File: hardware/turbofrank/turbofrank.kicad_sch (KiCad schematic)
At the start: 7 parts, among them CON2 UART, CON4 Power, J1 Main Jumper Set

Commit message: HW Rev 1.0
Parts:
- CON1: renamed from CON2; value UART -> Pin Header 1x03; AliExpress (none) -> https://www.aliexpress.com/item/1005007039504981.html
- CON2: renamed from CON4; value Power -> Pin Header 1x03; AliExpress (none) -> https://www.aliexpress.com/item/1005007039504981.html
- H1, H2, H3, H4: value MountingHole -> Hole 2.7mm
- J1: value Main Jumper Set -> Pin Header 2x18; AliExpress (none) -> https://www.aliexpress.com/item/1005006804478835.html
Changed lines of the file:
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@@
 	(title_block
 		(title "TurboFRANK")
-		(date "2025-01-28")
+		(date "2025-01-29")
 		(rev "1.0")
 		(company "Mikhail Matveev")
@@
 		(dnp no)
 		(fields_autoplaced yes)
-		(property "Reference" "#PWR0113"
+		(property "Reference" "#PWR05"
 			(at 201.93 102.87 0)
 			(effects
@@
 			(project ""
 				(path "/8c0b3d8b-46d3-4173-ab1e-a61765f77d61"
-					(reference "#PWR0113")
+					(reference "#PWR05")
 					(unit 1)
 				)
@@
 		(dnp no)
 		(fields_autoplaced yes)
-		(property "Reference" "CON2"
+		(property "Reference" "CON1"
 			(at 201.295 77.47 0)
 			(effects
@@
 			)
 		)
-		(property "Value" "UART"
+		(property "Value" "Pin Header 1x03"
 			(at 201.295 80.01 0)
 			(effects
@@
 			)
 		)
+		(property "AliExpress" "https://www.aliexpress.com/item/1005007039504981.html"
+			(at 200.66 85.09 0)
+			(effects
+				(font
+					(size 1.27 1.27)
+				)
+				(hide yes)
+			)
+		)
 		(pin "2"
 		)
@@
 			(project ""
 				(path "/8c0b3d8b-46d3-4173-ab1e-a61765f77d61"
-					(reference "CON2")
+					(reference "CON1")
 					(unit 1)
 				)
@@
 		(dnp no)
 		(fields_autoplaced yes)
-		(property "Reference" "#PWR0112"
+		(property "Reference" "#PWR03"
 			(at 201.93 97.79 0)
 			(effects
@@
 			(project ""
 				(path "/8c0b3d8b-46d3-4173-ab1e-a61765f77d61"
-					(reference "#PWR0112")
+					(reference "#PWR03")
 					(unit 1)
 				)
@@
 		(dnp no)
 		(fields_autoplaced yes)
-		(property "Reference" "#PWR0109"
+		(property "Reference" "#PWR02"
 			(at 212.09 82.55 0)
 			(effects
@@
 			(project ""
 				(path "/8c0b3d8b-46d3-4173-ab1e-a61765f77d61"
-					(reference "#PWR0109")
+					(reference "#PWR02")
 					(unit 1)
 				)
@@
 		(dnp no)
 		(fields_autoplaced yes)
-		(property "Reference" "#PWR0110"
+		(property "Reference" "#PWR04"
 			(at 212.09 100.33 0)
 			(effects
@@
 			(project ""
 				(path "/8c0b3d8b-46d3-4173-ab1e-a61765f77d61"
-					(reference "#PWR0110")
+					(reference "#PWR04")
 					(unit 1)
 				)
@@
 			)
 		)
-		(property "Value" "MountingHole"
+		(property "Value" "Hole 2.7mm"
 			(at 24.13 185.4199 0)
 			(effects
@@
 			)
 		)
-		(property "Value" "MountingHole"
+		(property "Value" "Hole 2.7mm"
 			(at 24.13 180.3399 0)
 			(effects
@@
 			)
 		)
-		(property "Value" "MountingHole"
+		(property "Value" "Hole 2.7mm"
 			(at 24.13 190.4999 0)
 			(effects
@@
 			)
 		)
-		(property "Value" "MountingHole"
+		(property "Value" "Hole 2.7mm"
 			(at 24.13 175.2599 0)
 			(effects
@@
 		(dnp no)
 		(fields_autoplaced yes)
-		(property "Reference" "CON4"
+		(property "Reference" "CON2"
 			(at 201.295 92.71 0)
 			(effects
@@
 			)
 		)
-		(property "Value" "Power"
+		(property "Value" "Pin Header 1x03"
 			(at 201.295 95.25 0)
 			(effects
@@
 			)
 		)
+		(property "AliExpress" "https://www.aliexpress.com/item/1005007039504981.html"
+			(at 200.66 100.33 0)
+			(effects
+				(font
+					(size 1.27 1.27)
+				)
+				(hide yes)
+			)
+		)
 		(pin "2"
 		)
@@
 			(project "turbofrank"
 				(path "/8c0b3d8b-46d3-4173-ab1e-a61765f77d61"
-					(reference "CON4")
+					(reference "CON2")
 					(unit 1)
 				)
@@
 			)
 		)
-		(property "Value" "Main Jumper Set"
+		(property "Value" "Pin Header 2x18"
 			(at 223.52 21.59 0)
 			(effects
@@
 			(at 222.25 45.72 0)
 			(effects
+				(font
+					(size 1.27 1.27)
+				)
+				(hide yes)
+			)
+		)
+		(property "AliExpress" "https://www.aliexpress.com/item/1005006804478835.html"
+			(at 222.25 45.72 0)
+			(effects

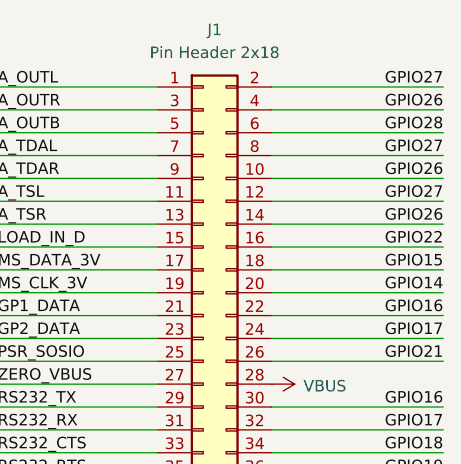
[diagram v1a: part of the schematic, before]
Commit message: Fixed audio pins
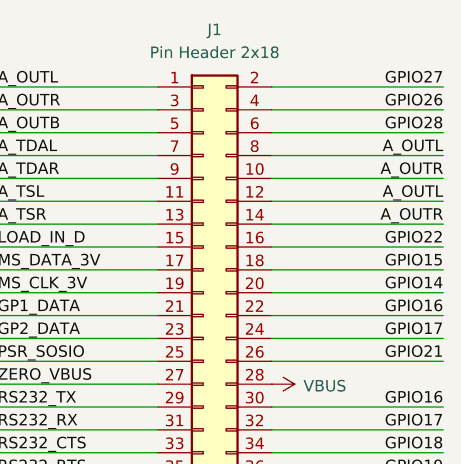
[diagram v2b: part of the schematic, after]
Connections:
- net A_OUTL: now also J1.12 (Pin_12), J1.8 (Pin_8)
- net A_OUTR: now also J1.10 (Pin_10), J1.14 (Pin_14)
- net GPIO26: no longer J1.10 (Pin_10), J1.14 (Pin_14)
- net GPIO27: no longer J1.12 (Pin_12), J1.8 (Pin_8)
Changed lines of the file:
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@@
 	(title_block
 		(title "TurboFRANK")
-		(date "2025-01-29")
-		(rev "1.0")
+		(date "2025-02-02")
+		(rev "1.01")
 		(company "Mikhail Matveev")
 		(comment 1 "https://github.com/xtremespb/frank")
@@
 		)
 	)
-	(label "GPIO26"
+	(label "A_OUTR"
 		(at 248.92 35.56 180)
 		(fields_autoplaced yes)
@@
 		)
 	)
-	(label "GPIO26"
+	(label "A_OUTR"
 		(at 248.92 40.64 180)
 		(fields_autoplaced yes)
@@
 		)
 	)
-	(label "GPIO27"
+	(label "A_OUTL"
 		(at 248.92 33.02 180)
 		(fields_autoplaced yes)
@@
 		)
 	)
-	(label "GPIO27"
+	(label "A_OUTL"
 		(at 248.92 38.1 180)
 		(fields_autoplaced yes)
